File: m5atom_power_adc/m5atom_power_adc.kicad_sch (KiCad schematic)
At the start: 112 parts, among them J1 USB_C_Receptacle_USB2.0_14P, J10 Conn_01x02, J11 Conn_01x02, J12 Conn_01x02, J13 Conn_01x02, J2 GROVE-CONNECTOR, J3 Conn_01x04_Pin, J4 Conn_01x02, J5 Conn_01x02, J6 Conn_01x02, J7 Conn_01x02, J8 Conn_01x02, J9 GROVE-CONNECTOR, Q1 AO3401A, Q2 MMBT2222A, Q3 MMBT2222A, Q4 MMBT2222A, Q5 AO3401A, Q6 MMBT2222A, Q7 MMBT2222A, SW1 Boot, SW2 Reset, U1 LM2596S-5, U2 ESP32-S3-MINI-1, U3 AMS1117-3.3, U4 ADS1115IDGS, U5 AMS1117-3.3

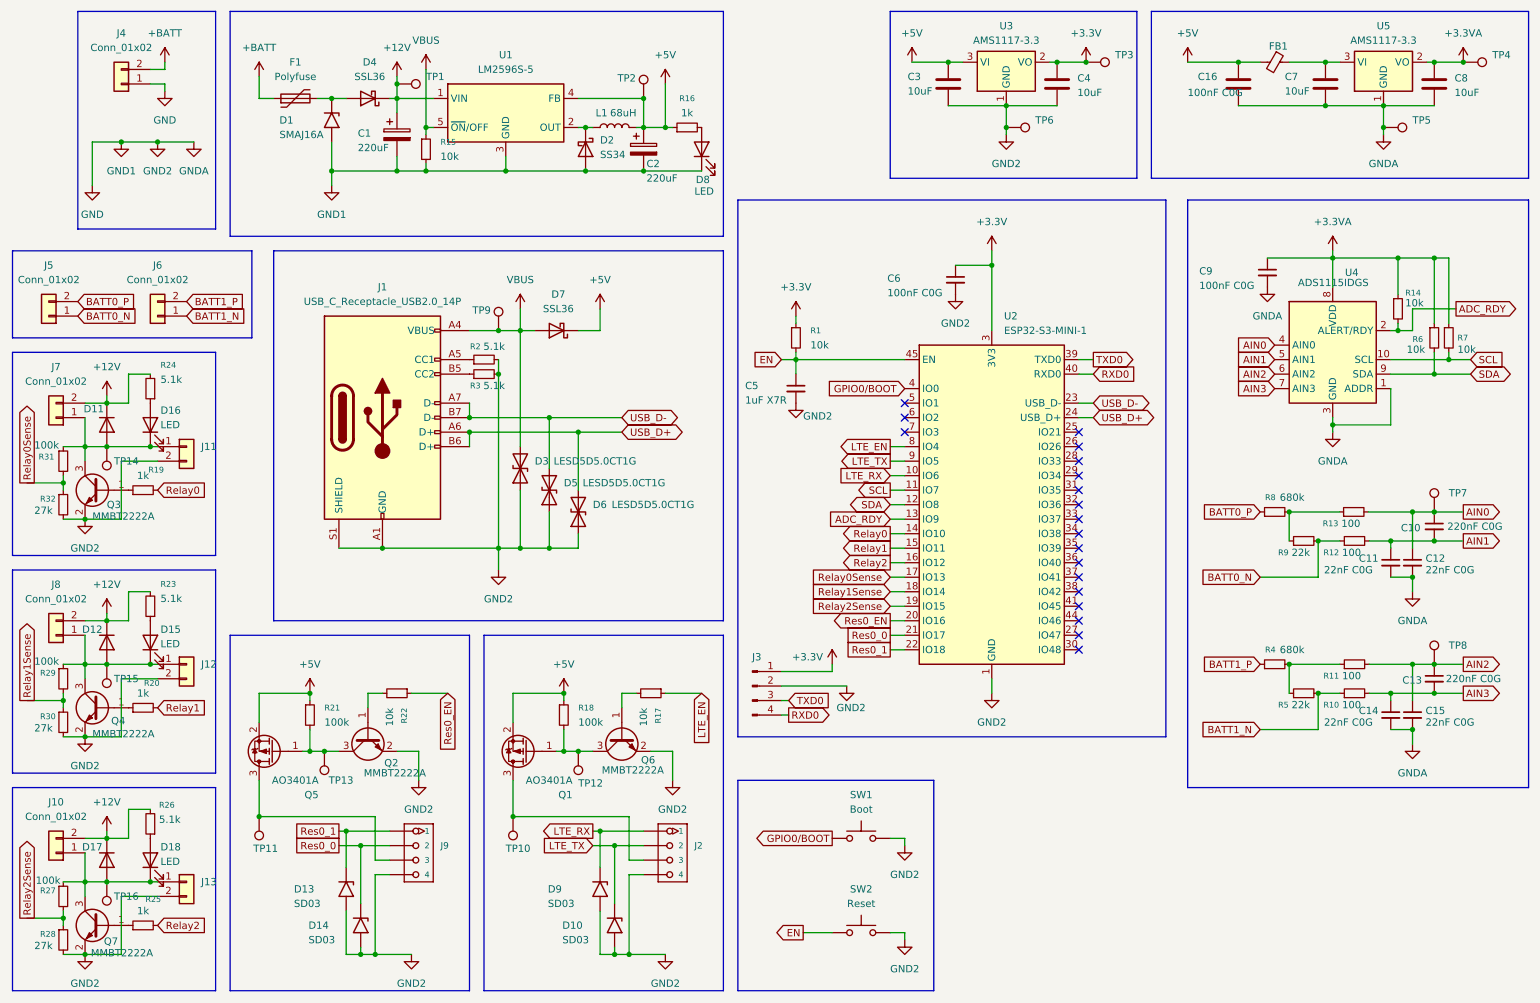
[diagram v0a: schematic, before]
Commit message: chore: 回路図更新・OBD2ドキュメント・MCP設定・エージェント基盤追加
Co-Authored-By: Claude Sonnet 4.6 <noreply@anthropic.com>
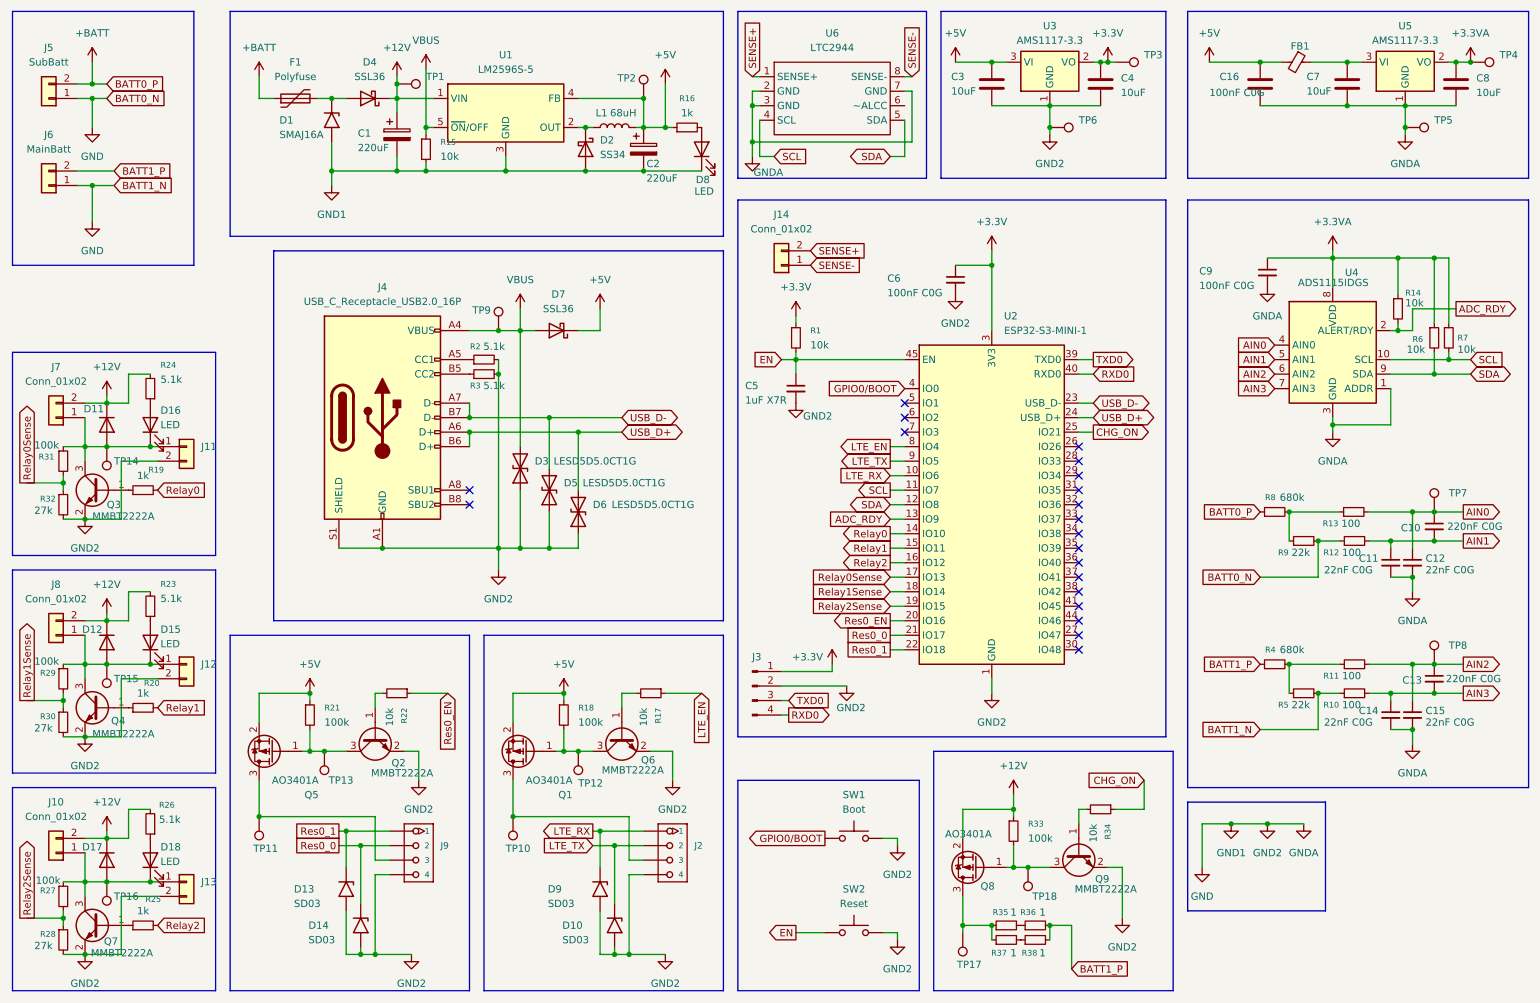
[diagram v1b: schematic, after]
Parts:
- removed J1: USB_C_Receptacle_USB2.0_14P, symbol Connector:USB_C_Receptacle_USB2.0_14P
- removed J4: Conn_01x02, symbol Connector_Generic:Conn_01x02
- added J14: Conn_01x02, symbol Connector_Generic:Conn_01x02
- added J4: USB_C_Receptacle_USB2.0_16P, Connector_USB:USB_C_Receptacle_HRO_TYPE-C-31-M-12, symbol Connector:USB_C_Receptacle_USB2.0_16P
- added Q8: AO3401A, Package_TO_SOT_SMD:SOT-23, symbol Transistor_FET:AO3401A
- added Q9: MMBT2222A, Package_TO_SOT_SMD:SOT-23, symbol Transistor_BJT:MMBT2222A
- added R33: 100k, symbol Device:R_Small
- added R34: 10k, symbol Device:R_Small
- added R35, R36, R37, R38: 1, symbol Device:R_Small
- added TP17, TP18: TestPoint, TestPoint:TestPoint_Pad_D1.5mm, symbol Connector:TestPoint
- added U6: LTC2944, symbol 000_my:LTC2944
- D15, D16, D18: footprint (none) -> LED_SMD:LED_0603_1608Metric; JLC_Num (none) -> C434558
- D8: footprint (none) -> LED_SMD:LED_0603_1608Metric; JLC_Num (none) -> C965804
- F1: footprint (none) -> Diode_SMD:D_SMB; JLC_Num (none) -> C19077571
- FB1: footprint (none) -> Inductor_SMD:L_0805_2012Metric; JLC_Num (none) -> C1017
- J5: value Conn_01x02 -> SubBatt
- J6: value Conn_01x02 -> MainBatt
- Q1, Q5: JLC_Num (none) -> C15127
- Q2, Q3, Q4, Q6, Q7: JLC_Num (none) -> C8512
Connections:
- net BATT0_N is gone; now on net GND: J5.1 (Pin_1), R12.1, R9.2
- net BATT0_P is gone; now on net +BATT: J5.2 (Pin_2), R8.1
- net BATT1_N is gone; now on net GND: J6.1 (Pin_1), R10.1, R5.2
- net +12V: now also Q8.2 (S), R33.1
- net BATT1_P: now also R36.2, R38.2
- net GND: now also J4.A1 (GND), J4.A12 (GND), J4.B1 (GND), J4.B12 (GND), J4.S1 (SHIELD), Q9.2 (E), U6.2 (GND), U6.3 (GND), U6.7 (GND)
- net SCL: now also U6.4 (SCL)
- net SDA: now also U6.5 (SDA)
- net USB_D+: now also J4.A6 (D+), J4.B6 (D+)
- net USB_D-: now also J4.A7 (D-), J4.B7 (D-)
- net VBUS: now also J4.A4 (VBUS), J4.A9 (VBUS), J4.B4 (VBUS), J4.B9 (VBUS)
- net at R2.1: now also J4.A5 (CC1)
- net at R3.1: now also J4.B5 (CC2)
- net CHG_ON: now reaches U2.25 (IO21)
- net CHG_ON: now also R34.1
- new net: Q8.1 (G), Q9.3 (C), R33.2, TP18.1
- new net: Q9.1 (B), R34.2
- new net: R37.2, R38.1
- new net: R35.2, R36.1
- new net: Q8.3 (D), R35.1, R37.1, TP17.1
- new net SENSE+: J14.2 (Pin_2), U6.1 (SENSE+)
- new net SENSE-: J14.1 (Pin_1), U6.8 (SENSE-)
- no-connect marks 19 -> 20
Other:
- moved on the sheet: C16, C3, C4, C7, C8, FB1, J5, J6, Q2, SW1, SW2, TP3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
